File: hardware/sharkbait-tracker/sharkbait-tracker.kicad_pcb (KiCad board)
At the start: 4 copper layers, 40.8 x 14 mm, 56 parts, among them J1 Conn_01x04, J2 Conn_Coaxial_Small, U1 Quectel_L96, U2 XC6206PxxxMR, U3 XT25F32FDTIGT, U4 LLCC68, U5 STM32L031G6Ux, Y1 32MHz

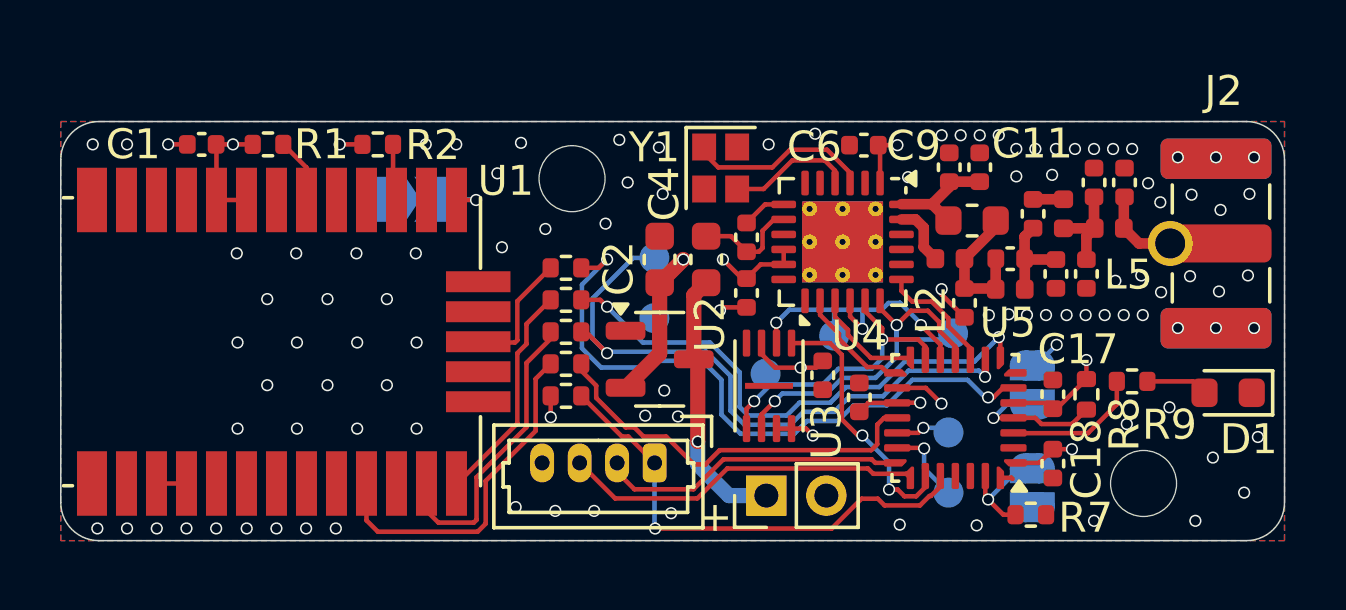
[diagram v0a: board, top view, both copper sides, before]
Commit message: Updated vias for easier tolerances
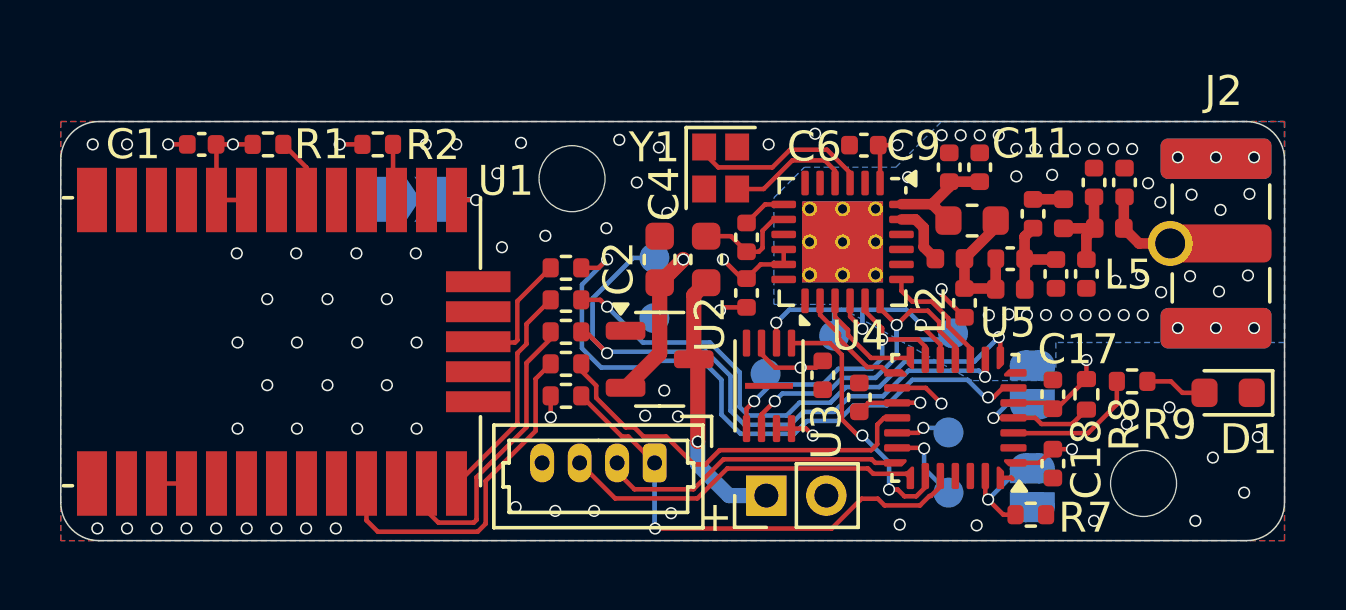
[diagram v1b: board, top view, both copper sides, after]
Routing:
- net GND: track 9.61 -> 8.64 mm, vias 103 -> 102
- added copper zone on B.Cu, net GND
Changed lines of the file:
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@@
 			(net 0)
 			(net_name "")
-			(layers "*.Cu")
+			(layers "F.Cu" "In1.Cu" "In2.Cu" "B.Cu")
 			(name "KEEPOUT_ANT")
 			(hatch edge 0.5)
@@
 			(at -1.1 -1.1 270)
 			(size 0.5 0.5)
-			(drill 0.2)
+			(drill 0.3048)
 			(property pad_prop_heatsink)
 			(layers "*.Cu")
@@
 			(at -1.1 0 270)
 			(size 0.5 0.5)
-			(drill 0.2)
+			(drill 0.3048)
 			(property pad_prop_heatsink)
 			(layers "*.Cu")
@@
 			(at -1.1 1.1 270)
 			(size 0.5 0.5)
-			(drill 0.2)
+			(drill 0.3048)
 			(property pad_prop_heatsink)
 			(layers "*.Cu")
@@
 			(at 0 -1.1 270)
 			(size 0.5 0.5)
-			(drill 0.2)
+			(drill 0.3048)
 			(property pad_prop_heatsink)
 			(layers "*.Cu")
@@
 			(at 0 0 270)
 			(size 0.5 0.5)
-			(drill 0.2)
+			(drill 0.3048)
 			(property pad_prop_heatsink)
 			(layers "*.Cu")
@@
 			(at 0 1.1 270)
 			(size 0.5 0.5)
-			(drill 0.2)
+			(drill 0.3048)
 			(property pad_prop_heatsink)
 			(layers "*.Cu")
@@
 			(at 1.1 -1.1 270)
 			(size 0.5 0.5)
-			(drill 0.2)
+			(drill 0.3048)
 			(property pad_prop_heatsink)
 			(layers "*.Cu")
@@
 			(at 1.1 0 270)
 			(size 0.5 0.5)
-			(drill 0.2)
+			(drill 0.3048)
 			(property pad_prop_heatsink)
 			(layers "*.Cu")
@@
 			(at 1.1 1.1 270)
 			(size 0.5 0.5)
-			(drill 0.2)
+			(drill 0.3048)
 			(property pad_prop_heatsink)
 			(layers "*.Cu")
@@
 	)
 	(via
-		(at 136.1694 78.8162)
-		(size 0.4064)
-		(drill 0.3048)
-		(layers "F.Cu" "B.Cu")
-		(net 3)
-	)
-	(via
 		(at 113.8428 80.1624)
 		(size 0.4064)
@@
 	)
 	(via
-		(at 121.1326 74.7776)
+		(at 121.158 74.93)
 		(size 0.4064)
 		(drill 0.3048)
@@
 	)
 	(via
-		(at 121.8692 73.406)
+		(at 122.174 73.406)
 		(size 0.4064)
 		(drill 0.3048)
@@
 	)
 	(via
-		(at 123.0376 73.787)
+		(at 123.19 74.422)
 		(size 0.4064)
 		(drill 0.3048)
@@
 	)
 	(via
-		(at 119.126 74.9554)
+		(at 119.126 75.184)
 		(size 0.4064)
 		(drill 0.3048)
@@
 	(segment
 		(start 135.4836 79.502)
-		(end 136.1694 78.8162)
+		(end 135.3566 79.502)
 		(width 0.1524)
 		(layer "B.Cu")
@@
 	)
 	(segment
-		(start 135.3566 79.502)
-		(end 135.4836 79.502)
+		(start 140.3604 80.4164)
+		(end 141.0969 80.4164)
 		(width 0.1524)
-		(layer "B.Cu")
-		(net 3)
+		(layer "F.Cu")
+		(net 4)
 	)
 	(segment
 		(start 139.194 80.0354)
-		(end 140.7159 80.0354)
+		(end 139.9794 80.0354)
 		(width 0.1524)
 		(layer "F.Cu")
@@
 	)
 	(segment
-		(start 140.7159 80.0354)
-		(end 141.0969 80.4164)
+		(start 139.9794 80.0354)
+		(end 140.3604 80.4164)
 		(width 0.1524)
 		(layer "F.Cu")
@@
 	)
 	(segment
-		(start 131.643574 78.109331)
-		(end 130.953443 77.4192)
-		(width 0.1524)
-		(layer "B.Cu")
-		(net 9)
-	)
-	(segment
-		(start 131.643574 78.160426)
-		(end 131.643574 78.109331)
+		(start 129.6924 77.6732)
+		(end 129.7178 77.6478)
 		(width 0.1524)
 		(layer "B.Cu")
@@
 	)
 	(segment
-		(start 129.6924 77.6732)
-		(end 129.7178 77.6478)
+		(start 127.254 77.6478)
+		(end 126.8222 78.0796)
 		(width 0.1524)
 		(layer "B.Cu")
@@
 	)
 	(segment
-		(start 127.254 77.6478)
-		(end 126.8222 78.0796)
+		(start 131.643574 78.160426)
+		(end 131.643574 78.133774)
 		(width 0.1524)
 		(layer "B.Cu")
@@
 	)
 	(segment
-		(start 130.560957 77.4232)
-		(end 130.336357 77.6478)
+		(start 131.1576 77.6478)
+		(end 129.7178 77.6478)
 		(width 0.1524)
 		(layer "B.Cu")
@@
 	)
 	(segment
-		(start 130.937 77.4192)
-		(end 130.933 77.4232)
-		(width 0.1524)
-		(layer "B.Cu")
-		(net 9)
-	)
-	(segment
-		(start 130.953443 77.4192)
-		(end 130.937 77.4192)
-		(width 0.1524)
-		(layer "B.Cu")
-		(net 9)
-	)
-	(segment
 		(start 129.7178 77.6478)
 		(end 128.8034 77.6478)
@@
 	)
 	(segment
-		(start 130.336357 77.6478)
-		(end 129.7178 77.6478)
-		(width 0.1524)
-		(layer "B.Cu")
-		(net 9)
-	)
-	(segment
-		(start 130.933 77.4232)
-		(end 130.560957 77.4232)
+		(start 131.643574 78.133774)
+		(end 131.1576 77.6478)
 		(width 0.1524)
 		(layer "B.Cu")
@@
 			)
 		)
+	)
+	(zone
+		(net 3)
+		(net_name "GND")
+		(layer "B.Cu")
+		(hatch edge 0.5)
+		(priority 4)
+		(connect_pads
+			(clearance 0.1524)
+		)
+		(min_thickness 0.1524)
+		(filled_areas_thickness no)
+		(fill yes
+			(thermal_gap 0.1524)
+			(thermal_bridge_width 0.254)
+		)
+		(polygon
+			(pts
+				(xy 127.762 72.898) (xy 130.81 72.898) (xy 132.334 71.374) (xy 143.764 71.374) (xy 143.764 78.74)
+				(xy 136.144 78.74) (xy 136.144 80.01) (xy 133.35 80.01) (xy 128.778 77.47) (xy 126.746 77.47) (xy 126.746 73.914)
+			)
+		)
